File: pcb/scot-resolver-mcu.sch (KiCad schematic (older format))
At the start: 31 parts, among them IC10 AD2S1210, IC9 STM32F0xxKxTx, J7 CONN_01x03, P1 SWD, Y1 Crystal_GND24, Y2 Crystal

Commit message: WIP..
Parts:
- added C69: 100n, Capacitor_SMD:C_0402_1005Metric, symbol Device:C
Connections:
- wire segments 155 -> 156
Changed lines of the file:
@@
 Wire Wire Line
 	7300 1050 7000 1050
+$Comp
+L Device:C C69
+U 1 1 5E4E05E5
+P 4650 6100
+F 0 "C69" H 4765 6146 50  0000 L CNN
+F 1 "100n" H 4765 6055 50  0000 L CNN
+F 2 "Capacitor_SMD:C_0402_1005Metric" H 4688 5950 50  0001 C CNN
+F 3 "~" H 4650 6100 50  0001 C CNN
+	1    4650 6100
+	1    0    0    -1
+$EndComp
+$Comp
+L power:GND #PWR0154
+U 1 1 5E4E18F6
+P 4650 6250
+F 0 "#PWR0154" H 4650 6000 50  0001 C CNN
+F 1 "GND" H 4655 6077 50  0000 C CNN
+F 2 "" H 4650 6250 50  0001 C CNN
+F 3 "" H 4650 6250 50  0001 C CNN
+	1    4650 6250
+	1    0    0    -1
+$EndComp
+Wire Wire Line
+	4650 5950 4500 5950
+Connection ~ 4500 5950
 $EndSCHEMATC

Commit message: WIP PCB v2.
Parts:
- C57, C58: value 12p -> 8p
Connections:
- net labels added: RD_nRESET
- wire segments 156 -> 157
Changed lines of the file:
@@
 P 2450 3450
 F 0 "C57" V 2702 3450 50  0000 C CNN
-F 1 "12p" V 2611 3450 50  0000 C CNN
+F 1 "8p" V 2611 3450 50  0000 C CNN
 F 2 "Capacitor_SMD:C_0402_1005Metric" H 2488 3300 50  0001 C CNN
 F 3 "~" H 2450 3450 50  0001 C CNN
@@
 P 2450 4100
 F 0 "C58" V 2198 4100 50  0000 C CNN
-F 1 "12p" V 2289 4100 50  0000 C CNN
+F 1 "8p" V 2289 4100 50  0000 C CNN
 F 2 "Capacitor_SMD:C_0402_1005Metric" H 2488 3950 50  0001 C CNN
 F 3 "~" H 2450 4100 50  0001 C CNN
@@
 	4650 5950 4500 5950
 Connection ~ 4500 5950
+Wire Wire Line
+	3250 4500 3650 4500
+Text Label 3250 4500 0    50   ~ 0
+RD_nRESET
+Text Label 8500 4550 0    50   ~ 0
+RD_nRESET
 $EndSCHEMATC

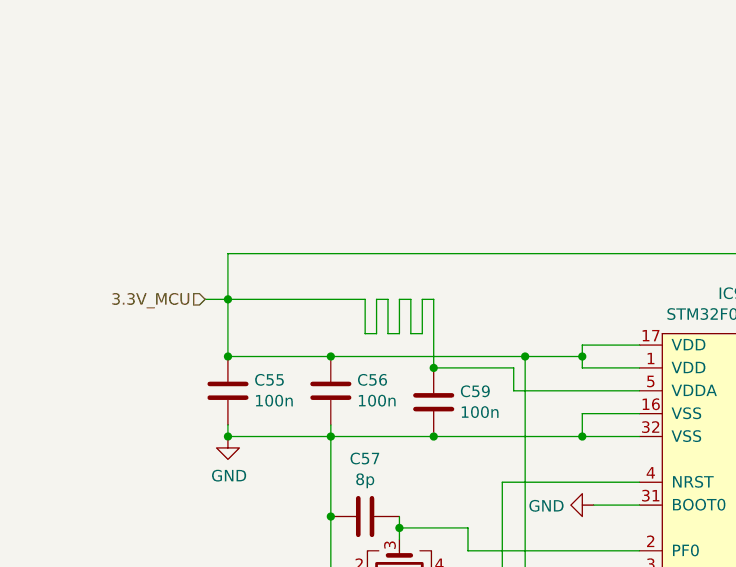
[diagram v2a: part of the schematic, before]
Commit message: pcb: V2 schematic updates (PCB still to do).
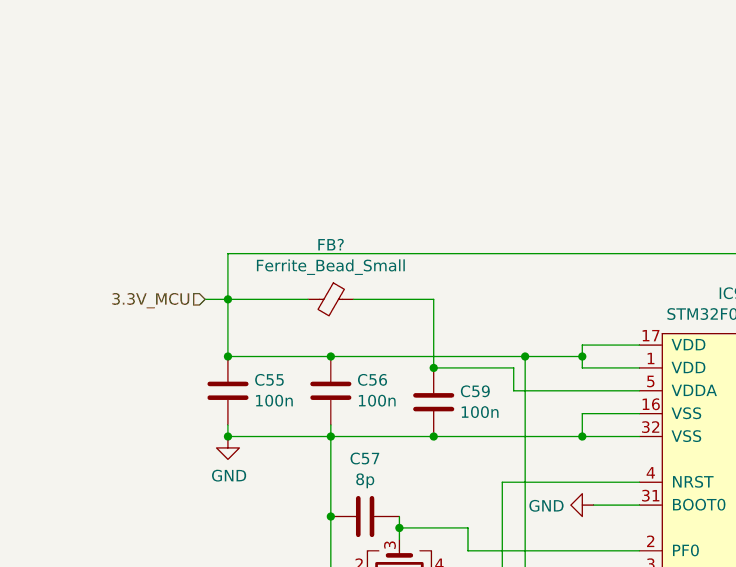
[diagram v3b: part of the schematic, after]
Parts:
- added FB?: Ferrite_Bead_Small, symbol Device:Ferrite_Bead_Small
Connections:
- wire segments 157 -> 146
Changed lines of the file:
@@
 $Descr A4 11693 8268
 encoding utf-8
-Sheet 9 9
+Sheet 7 7
 Title ""
 Date ""
@@
 Connection ~ 3400 2750
 Wire Wire Line
-	2750 2800 2750 2500
-Wire Wire Line
-	2750 2500 2700 2500
-Wire Wire Line
-	2700 2500 2700 2650
-Wire Wire Line
-	2700 2650 2650 2650
-Wire Wire Line
-	2650 2650 2650 2500
-Wire Wire Line
-	2650 2500 2600 2500
-Wire Wire Line
-	2600 2500 2600 2650
-Wire Wire Line
-	2600 2650 2550 2650
-Wire Wire Line
-	2550 2650 2550 2500
-Wire Wire Line
-	2550 2500 2500 2500
-Wire Wire Line
-	2500 2500 2500 2650
-Wire Wire Line
-	2500 2650 2450 2650
-Wire Wire Line
-	2450 2650 2450 2500
-Wire Wire Line
-	2450 2500 1850 2500
-Wire Wire Line
 	1850 2500 1850 2750
-Connection ~ 2750 2800
 Connection ~ 1850 2750
 Wire Wire Line
@@
 Text Label 8500 4550 0    50   ~ 0
 RD_nRESET
+$Comp
+L Device:Ferrite_Bead_Small FB?
+U 1 1 5EAA39FE
+P 2300 2500
+F 0 "FB?" V 2063 2500 50  0000 C CNN
+F 1 "Ferrite_Bead_Small" V 2154 2500 50  0000 C CNN
+F 2 "" V 2230 2500 50  0001 C CNN
+F 3 "~" H 2300 2500 50  0001 C CNN
+	1    2300 2500
+	0    1    1    0
+$EndComp
+Wire Wire Line
+	2750 2800 2750 2500
+Wire Wire Line
+	2750 2500 2400 2500
+Connection ~ 2750 2800
+Wire Wire Line
+	2200 2500 1850 2500
 $EndSCHEMATC

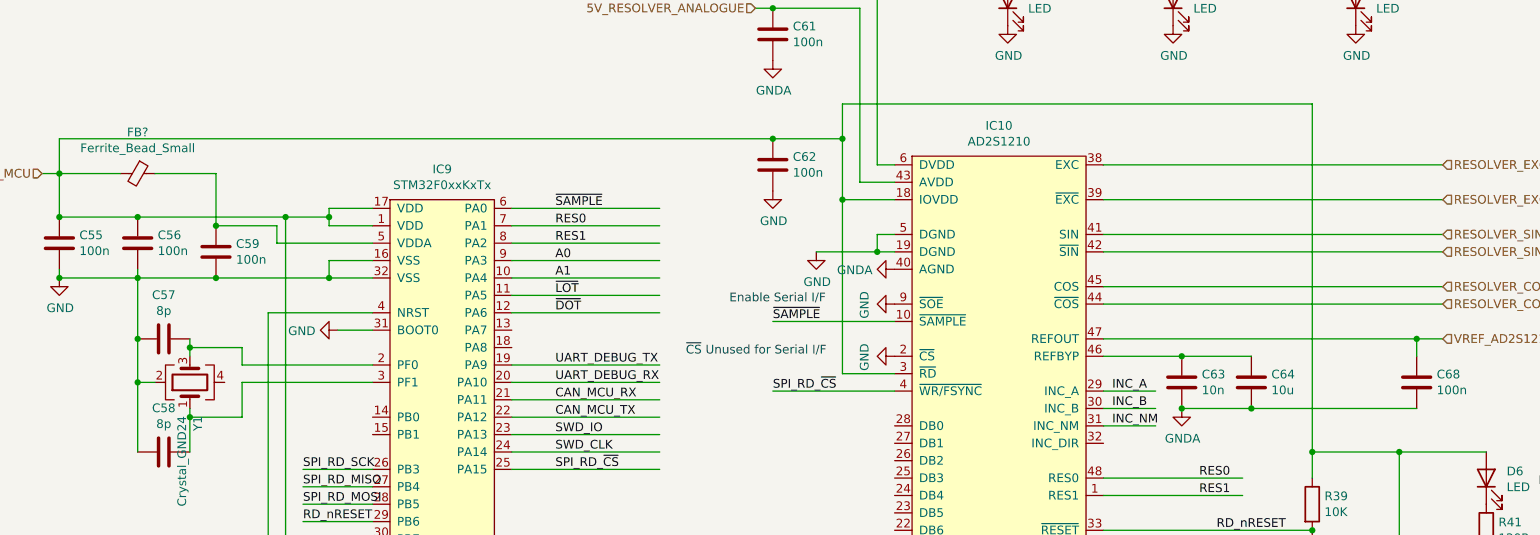
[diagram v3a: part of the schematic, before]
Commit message: pcb: Add 10u to VREF, all 0402->0603
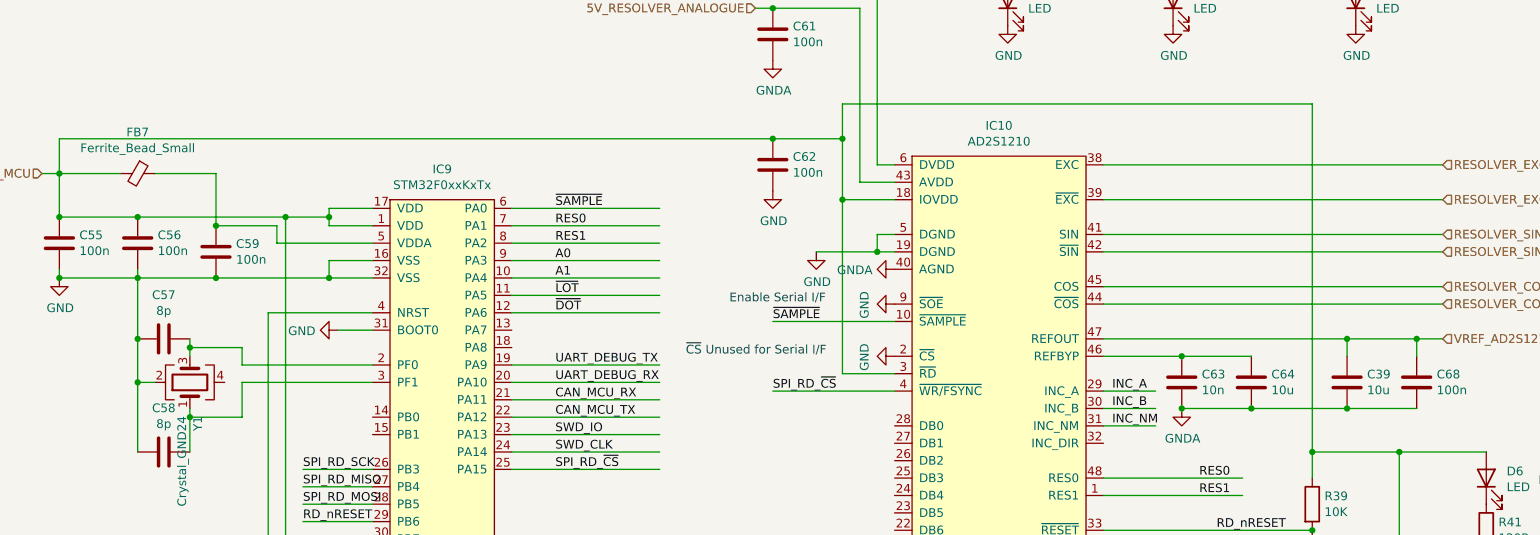
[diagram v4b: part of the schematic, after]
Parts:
- added C39: 10u, Capacitor_SMD:C_0603_1608Metric_Pad1.05x0.95mm_HandSolder, symbol Device:C
- C55, C56, C57, C58, C59, C60, C61, C62, C63, C65, C66, C67, C68, C69: footprint Capacitor_SMD:C_0402_1005Metric -> Capacitor_SMD:C_0603_1608Metric_Pad1.05x0.95mm_HandSolder
- FB7: renamed from FB?; footprint (none) -> Inductor_SMD:L_0805_2012Metric_Pad1.15x1.40mm_HandSolder
- R39: footprint Resistor_SMD:R_0402_1005Metric -> Resistor_SMD:R_0603_1608Metric_Pad1.05x0.95mm_HandSolder
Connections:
- wire segments 146 -> 149
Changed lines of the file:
@@
 F 0 "C62" H 6065 2496 50  0000 L CNN
 F 1 "100n" H 6065 2405 50  0000 L CNN
-F 2 "Capacitor_SMD:C_0402_1005Metric" H 5988 2300 50  0001 C CNN
+F 2 "Capacitor_SMD:C_0603_1608Metric_Pad1.05x0.95mm_HandSolder" H 5988 2300 50  0001 C CNN
 F 3 "~" H 5950 2450 50  0001 C CNN
 	1    5950 2450
@@
 F 0 "C55" H 1965 2946 50  0000 L CNN
 F 1 "100n" H 1965 2855 50  0000 L CNN
-F 2 "Capacitor_SMD:C_0402_1005Metric" H 1888 2750 50  0001 C CNN
+F 2 "Capacitor_SMD:C_0603_1608Metric_Pad1.05x0.95mm_HandSolder" H 1888 2750 50  0001 C CNN
 F 3 "~" H 1850 2900 50  0001 C CNN
 	1    1850 2900
@@
 F 0 "C56" H 2415 2946 50  0000 L CNN
 F 1 "100n" H 2415 2855 50  0000 L CNN
-F 2 "Capacitor_SMD:C_0402_1005Metric" H 2338 2750 50  0001 C CNN
+F 2 "Capacitor_SMD:C_0603_1608Metric_Pad1.05x0.95mm_HandSolder" H 2338 2750 50  0001 C CNN
 F 3 "~" H 2300 2900 50  0001 C CNN
 	1    2300 2900
@@
 F 0 "C59" H 2865 2996 50  0000 L CNN
 F 1 "100n" H 2865 2905 50  0000 L CNN
-F 2 "Capacitor_SMD:C_0402_1005Metric" H 2788 2800 50  0001 C CNN
+F 2 "Capacitor_SMD:C_0603_1608Metric_Pad1.05x0.95mm_HandSolder" H 2788 2800 50  0001 C CNN
 F 3 "~" H 2750 2950 50  0001 C CNN
 	1    2750 2950
@@
 F 0 "C57" V 2702 3450 50  0000 C CNN
 F 1 "8p" V 2611 3450 50  0000 C CNN
-F 2 "Capacitor_SMD:C_0402_1005Metric" H 2488 3300 50  0001 C CNN
+F 2 "Capacitor_SMD:C_0603_1608Metric_Pad1.05x0.95mm_HandSolder" H 2488 3300 50  0001 C CNN
 F 3 "~" H 2450 3450 50  0001 C CNN
 	1    2450 3450
@@
 F 0 "C58" V 2198 4100 50  0000 C CNN
 F 1 "8p" V 2289 4100 50  0000 C CNN
-F 2 "Capacitor_SMD:C_0402_1005Metric" H 2488 3950 50  0001 C CNN
+F 2 "Capacitor_SMD:C_0603_1608Metric_Pad1.05x0.95mm_HandSolder" H 2488 3950 50  0001 C CNN
 F 3 "~" H 2450 4100 50  0001 C CNN
 	1    2450 4100
@@
 F 0 "C67" H 9215 6096 50  0000 L CNN
 F 1 "18p" H 9215 6005 50  0000 L CNN
-F 2 "Capacitor_SMD:C_0402_1005Metric" H 9138 5900 50  0001 C CNN
+F 2 "Capacitor_SMD:C_0603_1608Metric_Pad1.05x0.95mm_HandSolder" H 9138 5900 50  0001 C CNN
 F 3 "~" H 9100 6050 50  0001 C CNN
 	1    9100 6050
@@
 F 0 "C65" H 8815 6096 50  0000 L CNN
 F 1 "18p" H 8815 6005 50  0000 L CNN
-F 2 "Capacitor_SMD:C_0402_1005Metric" H 8738 5900 50  0001 C CNN
+F 2 "Capacitor_SMD:C_0603_1608Metric_Pad1.05x0.95mm_HandSolder" H 8738 5900 50  0001 C CNN
 F 3 "~" H 8700 6050 50  0001 C CNN
 	1    8700 6050
@@
 F 0 "C66" H 9165 4746 50  0000 L CNN
 F 1 "100n" H 9165 4655 50  0000 L CNN
-F 2 "Capacitor_SMD:C_0402_1005Metric" H 9088 4550 50  0001 C CNN
+F 2 "Capacitor_SMD:C_0603_1608Metric_Pad1.05x0.95mm_HandSolder" H 9088 4550 50  0001 C CNN
 F 3 "~" H 9050 4700 50  0001 C CNN
 	1    9050 4700
@@
 F 0 "R39" H 9120 4446 50  0000 L CNN
 F 1 "10K" H 9120 4355 50  0000 L CNN
-F 2 "Resistor_SMD:R_0402_1005Metric" V 8980 4400 50  0001 C CNN
+F 2 "Resistor_SMD:R_0603_1608Metric_Pad1.05x0.95mm_HandSolder" V 8980 4400 50  0001 C CNN
 F 3 "~" H 9050 4400 50  0001 C CNN
 	1    9050 4400
@@
 F 0 "C63" H 8415 3746 50  0000 L CNN
 F 1 "10n" H 8415 3655 50  0000 L CNN
-F 2 "Capacitor_SMD:C_0402_1005Metric" H 8338 3550 50  0001 C CNN
+F 2 "Capacitor_SMD:C_0603_1608Metric_Pad1.05x0.95mm_HandSolder" H 8338 3550 50  0001 C CNN
 F 3 "~" H 8300 3700 50  0001 C CNN
 	1    8300 3700
@@
 F 0 "C68" H 9765 3746 50  0000 L CNN
 F 1 "100n" H 9765 3655 50  0000 L CNN
-F 2 "Capacitor_SMD:C_0402_1005Metric" H 9688 3550 50  0001 C CNN
+F 2 "Capacitor_SMD:C_0603_1608Metric_Pad1.05x0.95mm_HandSolder" H 9688 3550 50  0001 C CNN
 F 3 "~" H 9650 3700 50  0001 C CNN
 	1    9650 3700
@@
 	8300 3550 8700 3550
 Wire Wire Line
-	7850 3450 9650 3450
+	7850 3450 9250 3450
 Wire Wire Line
 	9650 3450 9650 3550
@@
 Connection ~ 8700 3850
 Wire Wire Line
-	8700 3850 9650 3850
+	8700 3850 9250 3850
 Wire Wire Line
 	7850 2450 9800 2450
@@
 F 0 "C60" H 6065 1046 50  0000 L CNN
 F 1 "100n" H 6065 955 50  0000 L CNN
-F 2 "Capacitor_SMD:C_0402_1005Metric" H 5988 850 50  0001 C CNN
+F 2 "Capacitor_SMD:C_0603_1608Metric_Pad1.05x0.95mm_HandSolder" H 5988 850 50  0001 C CNN
 F 3 "~" H 5950 1000 50  0001 C CNN
 	1    5950 1000
@@
 F 0 "C61" H 6065 1746 50  0000 L CNN
 F 1 "100n" H 6065 1655 50  0000 L CNN
-F 2 "Capacitor_SMD:C_0402_1005Metric" H 5988 1550 50  0001 C CNN
+F 2 "Capacitor_SMD:C_0603_1608Metric_Pad1.05x0.95mm_HandSolder" H 5988 1550 50  0001 C CNN
 F 3 "~" H 5950 1700 50  0001 C CNN
 	1    5950 1700
@@
 F 0 "C69" H 4765 6146 50  0000 L CNN
 F 1 "100n" H 4765 6055 50  0000 L CNN
-F 2 "Capacitor_SMD:C_0402_1005Metric" H 4688 5950 50  0001 C CNN
+F 2 "Capacitor_SMD:C_0603_1608Metric_Pad1.05x0.95mm_HandSolder" H 4688 5950 50  0001 C CNN
 F 3 "~" H 4650 6100 50  0001 C CNN
 	1    4650 6100
@@
 RD_nRESET
 $Comp
-L Device:Ferrite_Bead_Small FB?
+L Device:Ferrite_Bead_Small FB7
 U 1 1 5EAA39FE
 P 2300 2500
-F 0 "FB?" V 2063 2500 50  0000 C CNN
+F 0 "FB7" V 2063 2500 50  0000 C CNN
 F 1 "Ferrite_Bead_Small" V 2154 2500 50  0000 C CNN
-F 2 "" V 2230 2500 50  0001 C CNN
+F 2 "Inductor_SMD:L_0805_2012Metric_Pad1.15x1.40mm_HandSolder" V 2230 2500 50  0001 C CNN
 F 3 "~" H 2300 2500 50  0001 C CNN
 	1    2300 2500
@@
 Wire Wire Line
 	2200 2500 1850 2500
+$Comp
+L Device:C C39
+U 1 1 5EA813F1
+P 9250 3700
+F 0 "C39" H 9365 3746 50  0000 L CNN
+F 1 "10u" H 9365 3655 50  0000 L CNN
+F 2 "Capacitor_SMD:C_0603_1608Metric_Pad1.05x0.95mm_HandSolder" H 9288 3550 50  0001 C CNN
+F 3 "~" H 9250 3700 50  0001 C CNN
+	1    9250 3700
+	1    0    0    -1
+$EndComp
+Connection ~ 9250 3850
+Wire Wire Line
+	9250 3850 9650 3850
+Wire Wire Line
+	9250 3550 9250 3450
+Connection ~ 9250 3450
+Wire Wire Line
+	9250 3450 9650 3450
 $EndSCHEMATC

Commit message: pcb: Progress on v2 layout.
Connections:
- net labels added: 0V_ANALOGUE, 0V_DIGITAL
- wire segments 149 -> 153
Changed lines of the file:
@@
 Wire Wire Line
 	9250 3450 9650 3450
+$Comp
+L power:GND #PWR0116
+U 1 1 5ED090A2
+P 3700 1150
+F 0 "#PWR0116" H 3700 900 50  0001 C CNN
+F 1 "GND" H 3705 977 50  0000 C CNN
+F 2 "" H 3700 1150 50  0001 C CNN
+F 3 "" H 3700 1150 50  0001 C CNN
+	1    3700 1150
+	1    0    0    -1
+$EndComp
+Wire Wire Line
+	3600 1050 3700 1050
+Wire Wire Line
+	3700 1050 3700 1150
+$Comp
+L power:GNDA #PWR0117
+U 1 1 5ED16E05
+P 3700 1700
+F 0 "#PWR0117" H 3700 1450 50  0001 C CNN
+F 1 "GNDA" H 3705 1527 50  0000 C CNN
+F 2 "" H 3700 1700 50  0001 C CNN
+F 3 "" H 3700 1700 50  0001 C CNN
+	1    3700 1700
+	1    0    0    -1
+$EndComp
+Text HLabel 3600 1600 0    50   Input ~ 0
+0V_ANALOGUE
+Wire Wire Line
+	3600 1600 3700 1600
+Wire Wire Line
+	3700 1600 3700 1700
+Text HLabel 3600 1050 0    50   Input ~ 0
+0V_DIGITAL
 $EndSCHEMATC

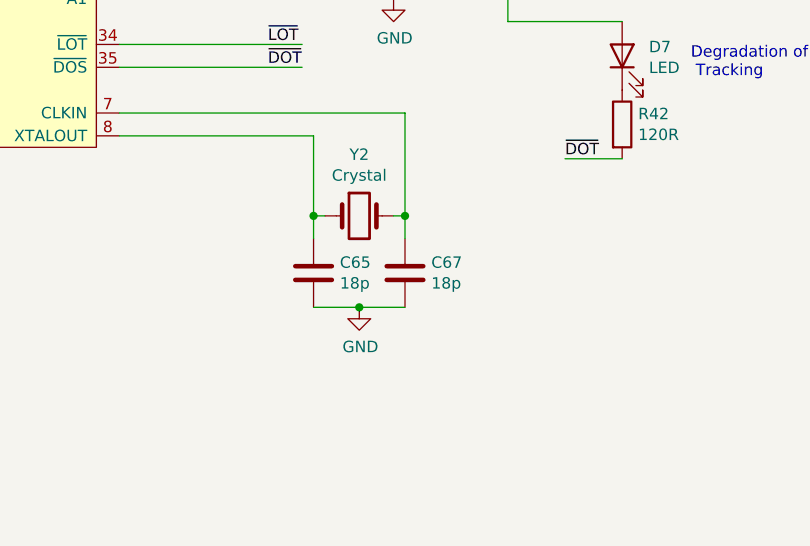
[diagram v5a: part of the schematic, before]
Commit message: pcb: Add v2 BOM, fix some component values.
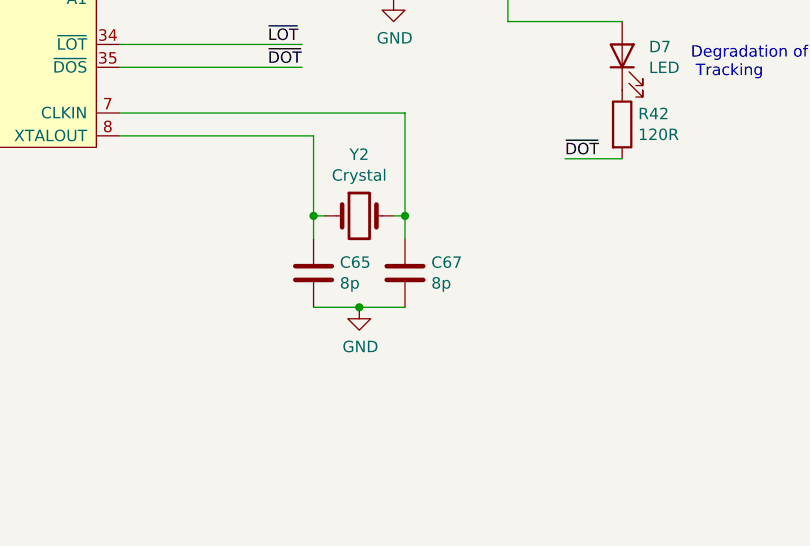
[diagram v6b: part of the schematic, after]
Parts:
- C65, C67: value 18p -> 8p
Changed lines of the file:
@@
 $Descr A4 11693 8268
 encoding utf-8
-Sheet 7 7
+Sheet 6 7
 Title ""
 Date ""
@@
 P 9100 6050
 F 0 "C67" H 9215 6096 50  0000 L CNN
-F 1 "18p" H 9215 6005 50  0000 L CNN
+F 1 "8p" H 9215 6005 50  0000 L CNN
 F 2 "Capacitor_SMD:C_0603_1608Metric_Pad1.05x0.95mm_HandSolder" H 9138 5900 50  0001 C CNN
 F 3 "~" H 9100 6050 50  0001 C CNN
@@
 P 8700 6050
 F 0 "C65" H 8815 6096 50  0000 L CNN
-F 1 "18p" H 8815 6005 50  0000 L CNN
+F 1 "8p" H 8815 6005 50  0000 L CNN
 F 2 "Capacitor_SMD:C_0603_1608Metric_Pad1.05x0.95mm_HandSolder" H 8738 5900 50  0001 C CNN
 F 3 "~" H 8700 6050 50  0001 C CNN
